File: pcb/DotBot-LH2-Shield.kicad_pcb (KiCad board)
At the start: 4 copper layers, 29 x 27 mm, 23 parts, among them J1 Conn_01x04, J2 Conn_01x10, J3 Conn_01x10, Q1 NX6008NBKWX, Q2 NX6008NBKWX, Q3 NX6008NBKWX, U1 ISM330DHCXTR, U2 TS4231, U4 LIS3MDL

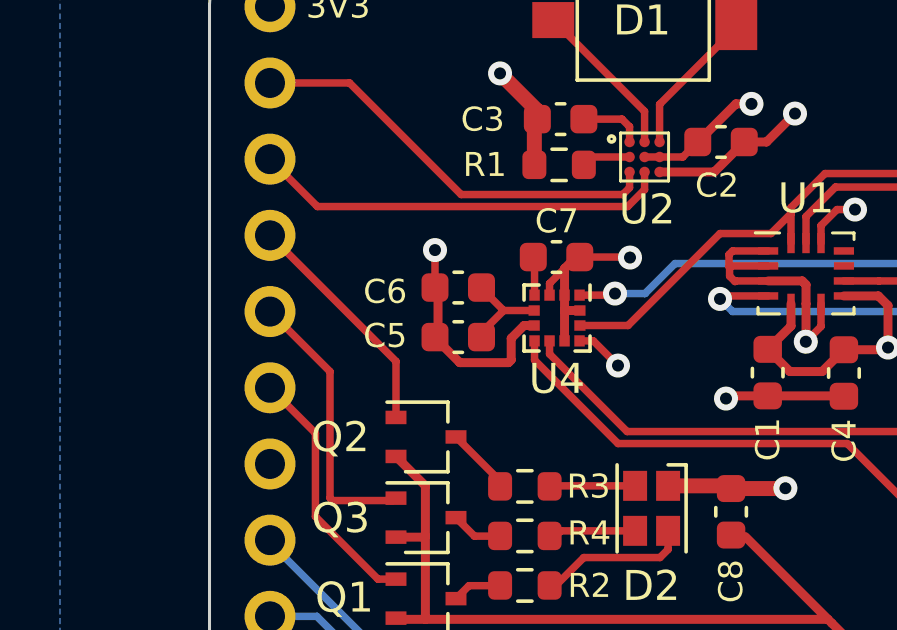
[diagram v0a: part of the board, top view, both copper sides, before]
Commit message: LH2 shield: fix LIS3MDL setup
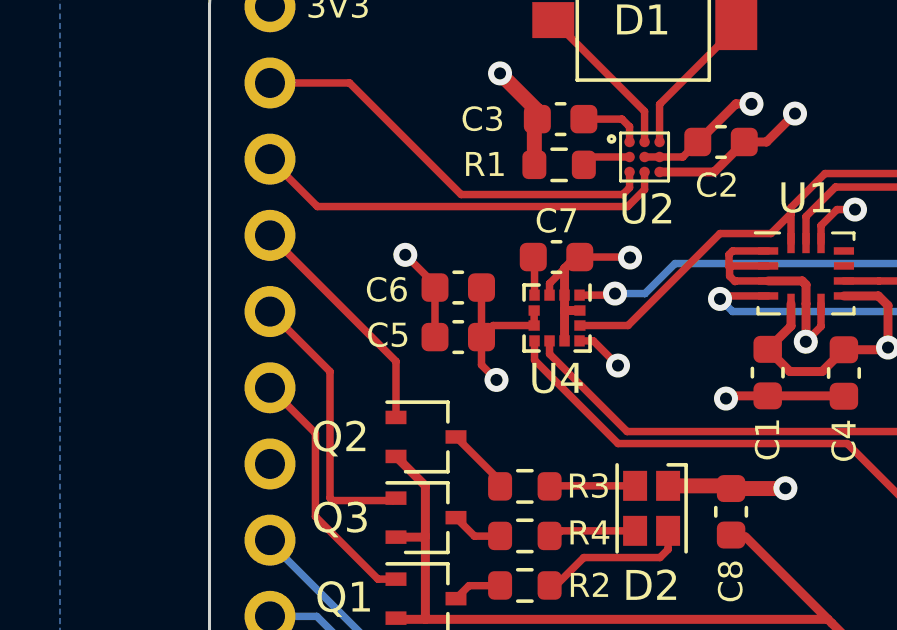
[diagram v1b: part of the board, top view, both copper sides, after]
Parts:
- turned C5 to 180 degrees
- turned C6 to 180 degrees
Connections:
- C5 pad 2: Net-(U4-Vdd) -> GND
- C6 pad 2: Net-(U4-Vdd) -> GND
- U4 pad 5: Net-(U4-Vdd) -> +3V3
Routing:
- net Net-(U4-Vdd): track 3.20 -> 0.00 mm
- net GND: track 60.5 -> 63.6 mm, vias 5 -> 6
- net +3V3: track 25.7 -> 24.1 mm
